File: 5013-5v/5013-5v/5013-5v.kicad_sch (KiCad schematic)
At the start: 24 parts, among them IC1 LM5013DDAR, J1 Conn_01x02_Pin, J2 Conn_01x02_Pin, J4 Conn_01x02_Pin, U1 LT1084-5.0

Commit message: added regulators, rough layout
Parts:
- removed C1: 10uF, symbol Device:C_Polarized
- removed C2: 10uF_tantalum, symbol Device:C_Polarized
- removed J2: Conn_01x02_Pin, Connector_PinHeader_2.54mm:PinHeader_1x02_P2.54mm_Vertical, symbol Connector:Conn_01x02_Pin
- removed R: 121, Resistor_SMD:R_0603_1608Metric_Pad0.98x0.95mm_HandSolder, symbol Device:R
- removed R1: R_Variable, symbol Device:R_Variable
- removed R2: 0, Resistor_SMD:R_0603_1608Metric_Pad0.98x0.95mm_HandSolder, symbol Device:R
- removed U1: LT1084-5.0, symbol Regulator_Linear:LT1084-5.0
- removed V1: 1, symbol Simulation_SPICE:VDC
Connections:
- net 0 renamed GND
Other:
- added sheet regulators (5013-5v_regulators.kicad_sch)

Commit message: 5013 rough layout complete
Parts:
- added C8, C9: C_Polarized, Capacitor_THT:CP_Radial_D5.0mm_P2.00mm, symbol Device:C_Polarized
- added R5: 2.2k, Resistor_SMD:R_0603_1608Metric_Pad0.98x0.95mm_HandSolder, symbol Device:R
- added pgood1: LED, LED_SMD:LED_0603_1608Metric_Pad1.05x0.95mm_HandSolder, symbol Device:LED
- renumbered J4 to J2
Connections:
- net GND: now also C8.2, C9.2, pgood1.1 (K)
- net Vin: now also C8.1, C9.1
- net at IC1.6 (PGOOD): now also R5.2
- new net: R5.1, pgood1.2 (A)
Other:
- note added: "optional THT electro caps"
- moved on the sheet: J1

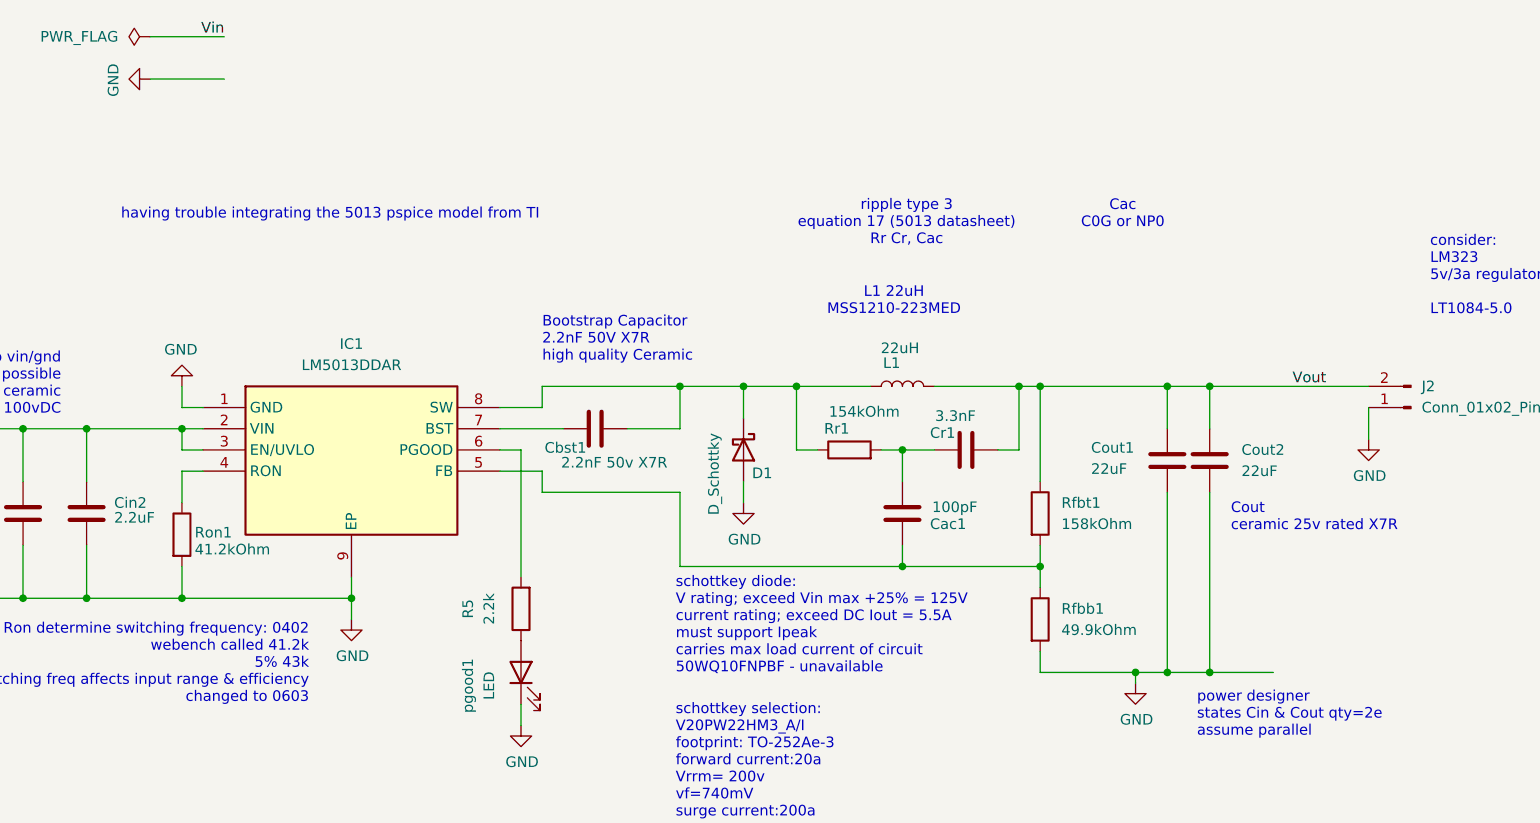
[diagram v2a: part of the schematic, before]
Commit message: routed pcbnew, gathering bom
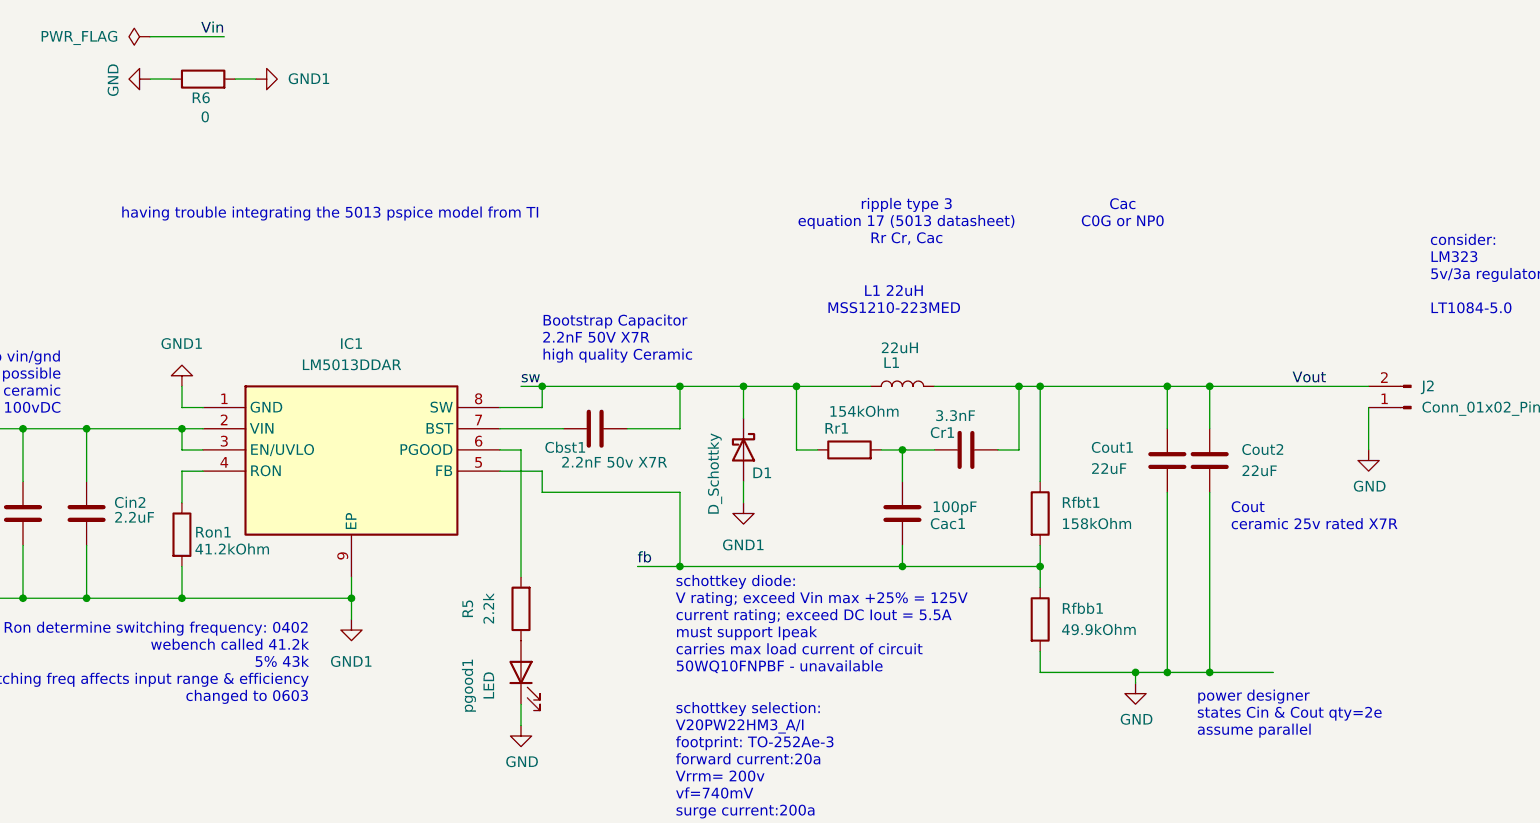
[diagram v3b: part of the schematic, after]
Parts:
- added R6: 0, Resistor_SMD:R_0603_1608Metric_Pad0.98x0.95mm_HandSolder, symbol Device:R
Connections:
- net GND: now also R6.1; no longer C8.2, C9.2, Cin1.2, Cin2.2, D1.2 (A), IC1.1 (GND), IC1.9 (EP), J1.2 (Pin_2), Ron1.2
- net fb: now reaches Cac1.2, IC1.5 (FB), Rfbb1.1, Rfbt1.2
- net sw: now reaches Cbst1.1, D1.1 (K), IC1.8 (SW), L1.1, Rr1.1
- new net GND1: C8.2, C9.2, Cin1.2, Cin2.2, D1.2 (A), IC1.1 (GND), IC1.9 (EP), J1.2 (Pin_2), R6.2, Ron1.2

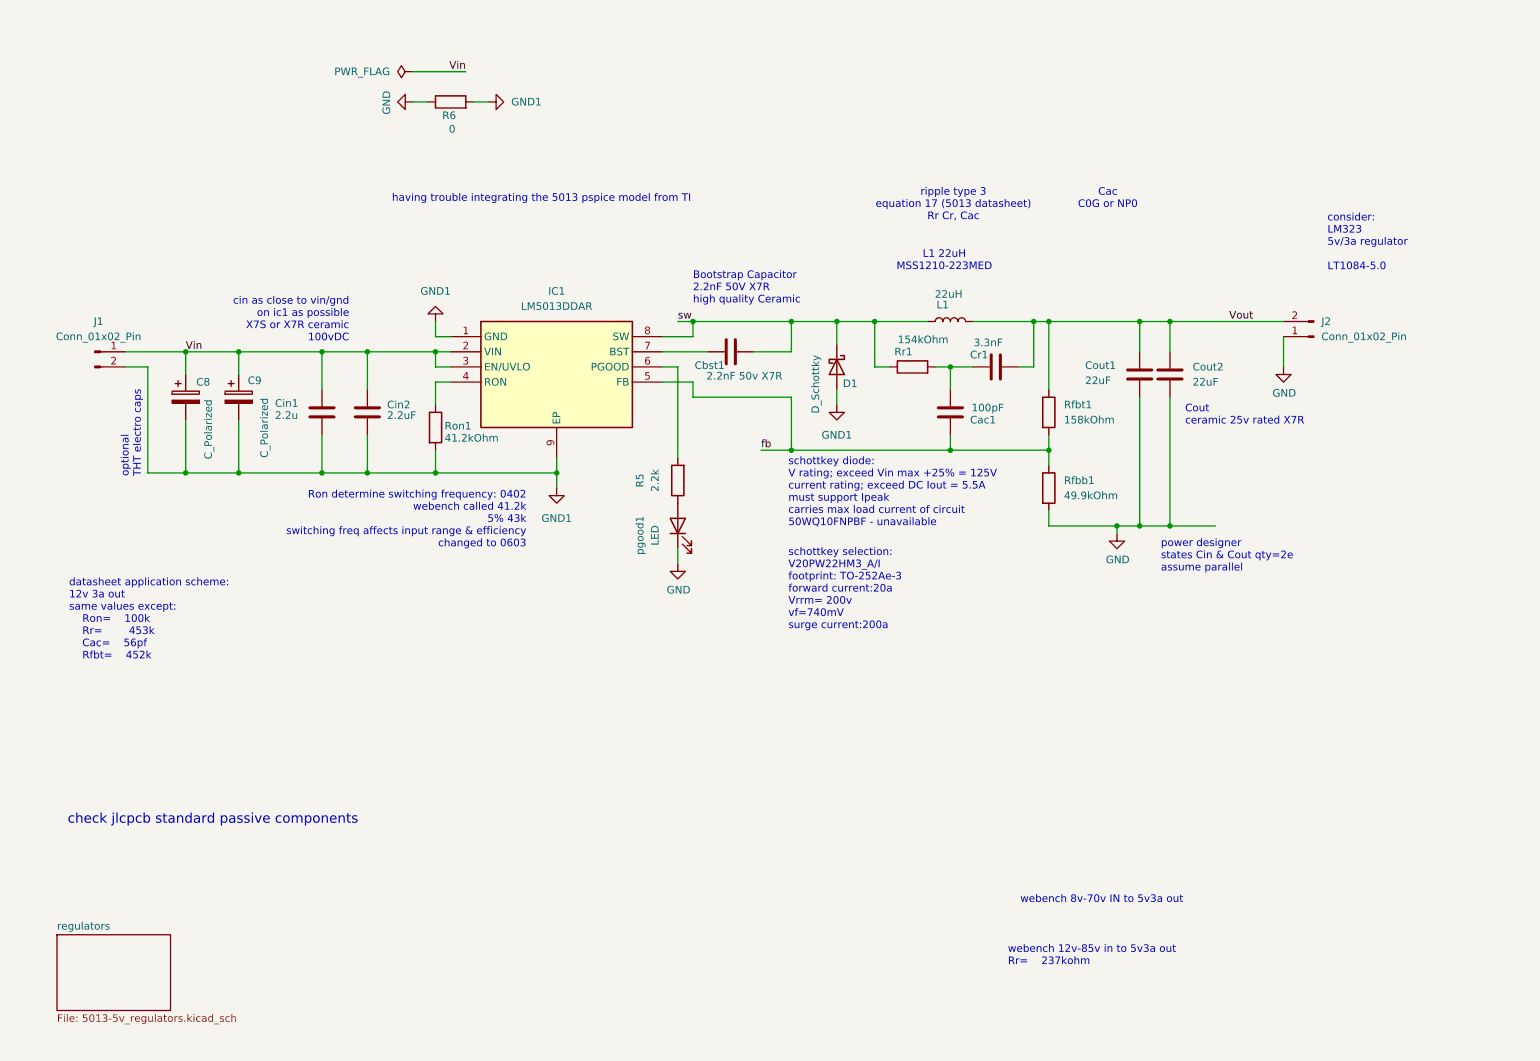
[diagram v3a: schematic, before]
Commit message: added rev1BOM, fixed pours
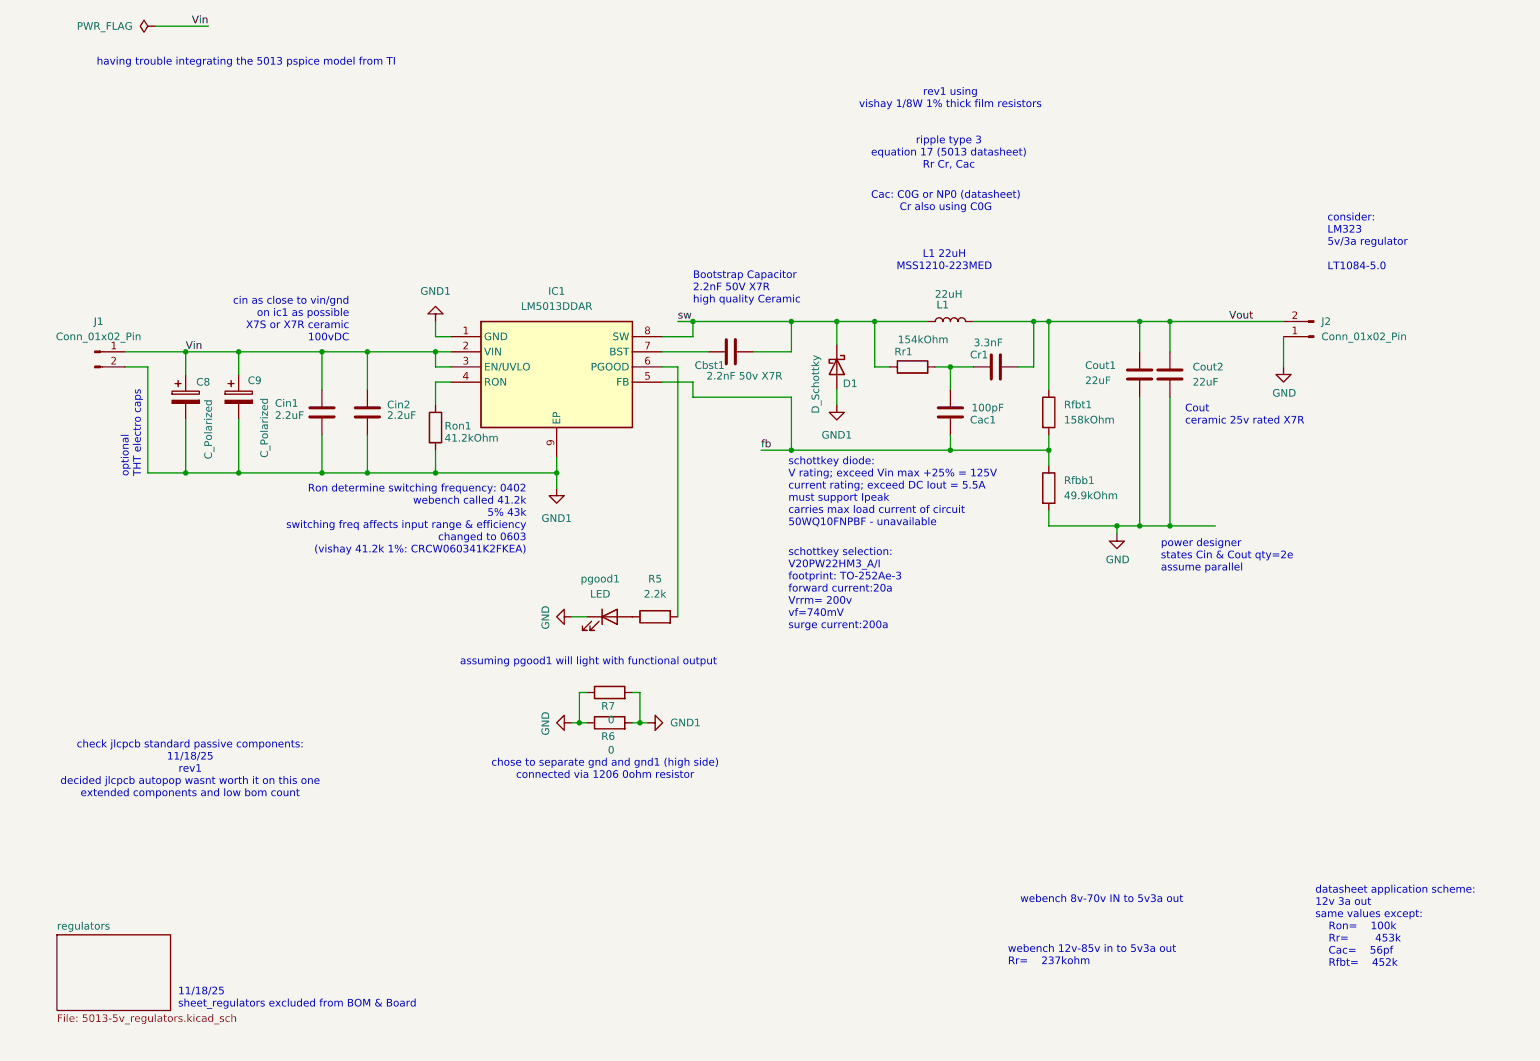
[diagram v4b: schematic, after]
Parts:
- added R7: 0, Resistor_SMD:R_1206_3216Metric_Pad1.30x1.75mm_HandSolder, symbol Device:R
- Cin1: value 2.2u -> 2.2uF
- R6: footprint Resistor_SMD:R_0603_1608Metric_Pad0.98x0.95mm_HandSolder -> Resistor_SMD:R_1206_3216Metric_Pad1.30x1.75mm_HandSolder
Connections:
- net GND: now also R7.1
- net GND1: now also R7.2
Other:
- note added: "11/18/25 sheet_regulators excluded from BOM & Board"
- note added: "Cac: C0G or NP0 (datasheet) Cr also using C0G"
- note added: "Ron determine switching frequency: 0402 webench called 41.2k 5% 43k switching freq affects input range & efficiency changed to 0603 (vishay 41.2k 1%: CRCW060341K2FKEA)"
- note added: "assuming pgood1 will light with functional output"
- note added: "check jlcpcb standard passive components: 11/18/25 rev1 decided jlcpcb autopop wasnt worth it on this one extended components and low bom count"
- note added: "chose to separate gnd and gnd1 (high side) connected via 1206 0ohm resistor"
- note added: "rev1 using vishay 1/8W 1% thick film resistors"
- note removed: "Cac C0G or NP0"
- note removed: "Ron determine switching frequency: 0402 webench called 41.2k 5% 43k switching freq affects input range & efficiency changed to 0603"
- note removed: "check jlcpcb standard passive components"
- moved on the sheet: R5, R6, pgood1

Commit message: plotted rev1 gerbers
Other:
- note added: "11/18/25 bom:5013-5-rev1-part#.csv imported to mouser estimated bom cost: 16.13+2.71 tariff"
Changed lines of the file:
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@@
 	(generator_version "9.0")
 	(paper "A4")
+	(text "11/18/25\nbom:5013-5-rev1-part#.csv imported to mouser\nestimated bom cost: 16.13+2.71 tariff"
+		(exclude_from_sim no)
+		(at 173.99 191.262 0)
+		(effects
+			(font
+				(size 1.27 1.27)
+			)
+			(justify right)
+		)
+	)
 	(text "optional \nTHT electro caps"
 		(exclude_from_sim no)
